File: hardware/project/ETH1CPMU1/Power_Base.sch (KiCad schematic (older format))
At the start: 16 parts, among them Q501 IRFR5410, U501 LM1117IMP-3.3/NOPB, U502 TSR1-2450, U503 MAX5902

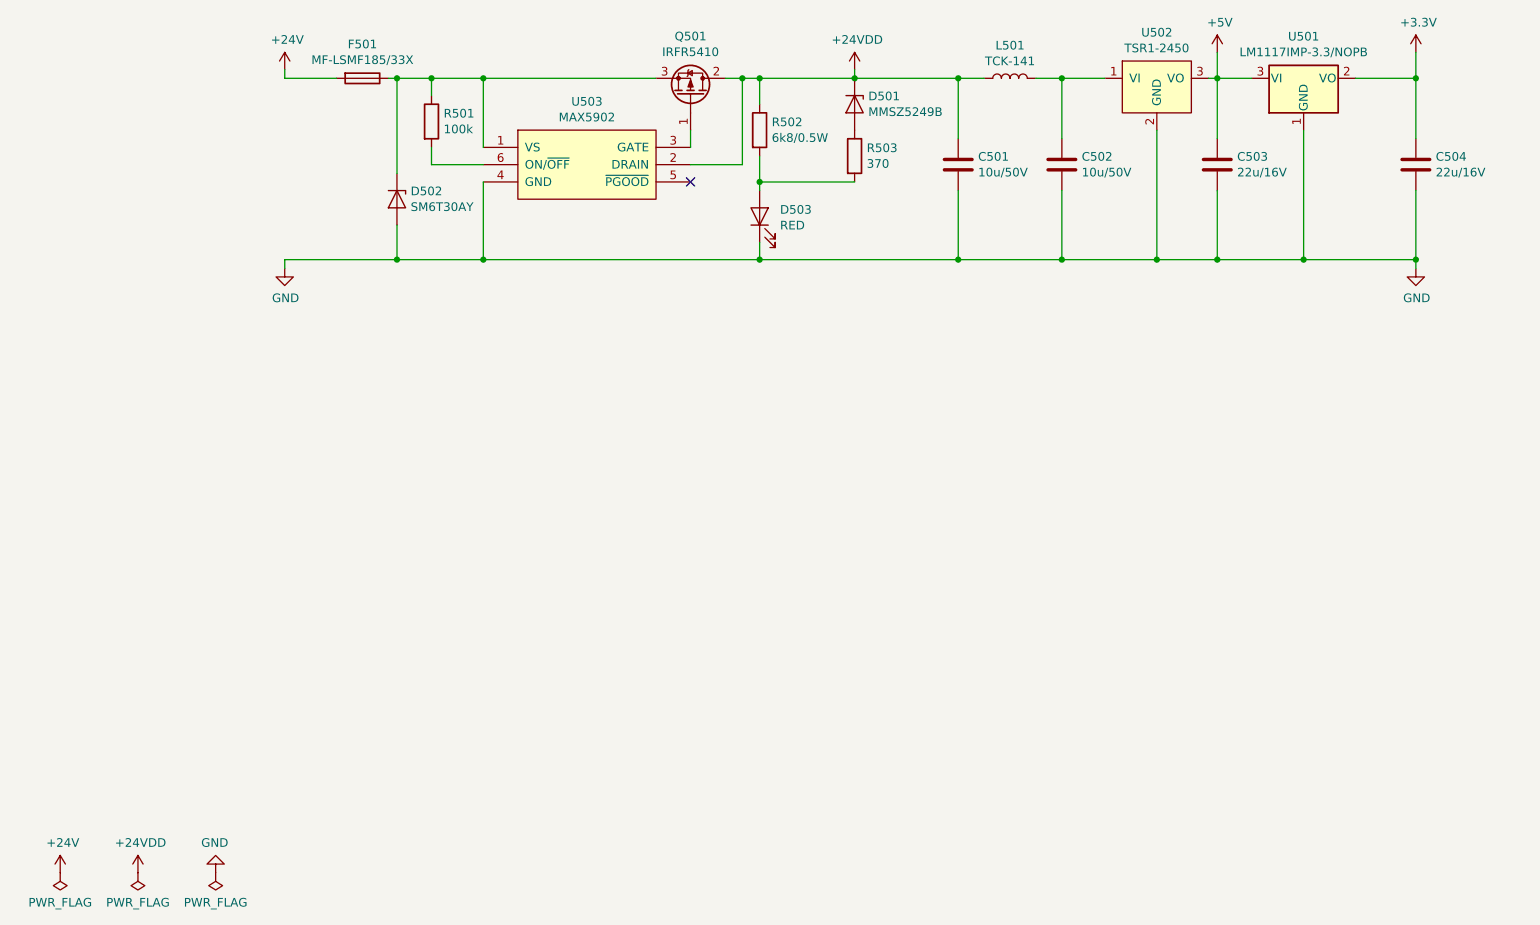
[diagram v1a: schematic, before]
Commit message: Function generator schematic design.
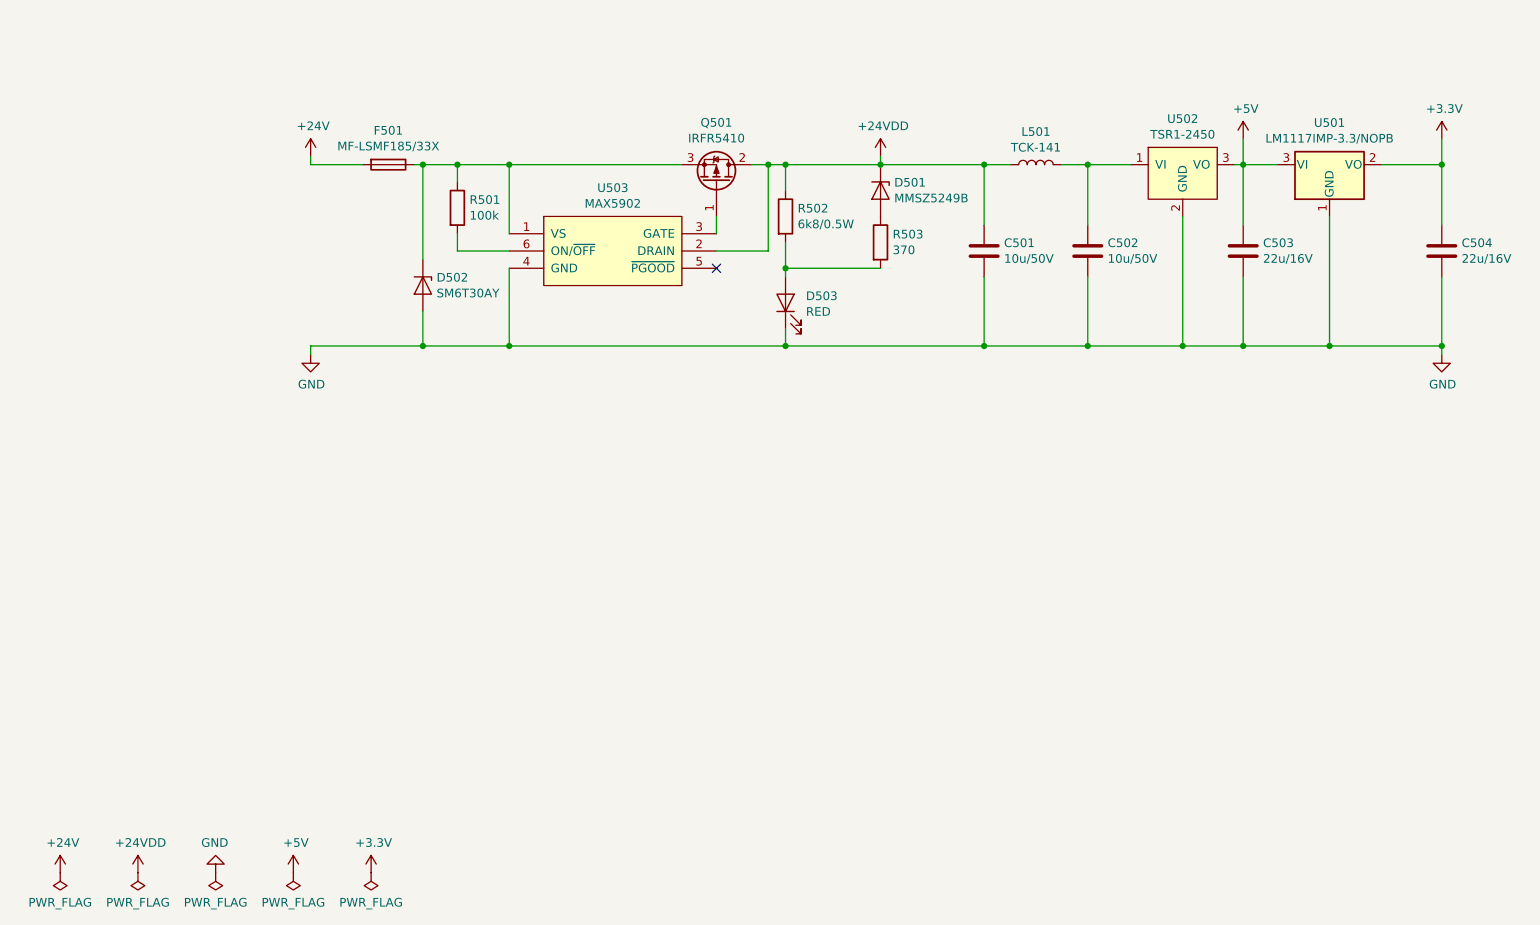
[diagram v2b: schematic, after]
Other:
- moved on the sheet: C501, C502, C503, C504, D501, D502, D503, F501, L501, Q501, R501, R502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

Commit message: Schematic and PCB design.
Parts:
- C501, C502: footprint Capacitor_SMD:C_2220_5650Metric_Pad1.97x5.40mm_HandSolder -> Capacitor_SMD:C_1206_3216Metric_Pad1.42x1.75mm_HandSolder
- C503, C504: value 22u/16V -> 10u/16V; footprint Capacitor_SMD:C_2220_5650Metric_Pad1.97x5.40mm_HandSolder -> Capacitor_SMD:C_1206_3216Metric_Pad1.42x1.75mm_HandSolder
- U502: footprint (none) -> ETH1CPMU1:TSR1

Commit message: Schematic design
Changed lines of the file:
@@
 Wire Wire Line
 	6850 3200 6850 3250
+$Comp
+L power:PWR_FLAG #FLG0502
+U 1 1 5DDE91B3
+P 850 7350
+F 0 "#FLG0502" H 850 7425 50  0001 C CNN
+F 1 "PWR_FLAG" H 850 7523 50  0000 C CNN
+F 2 "" H 850 7350 50  0001 C CNN
+F 3 "~" H 850 7350 50  0001 C CNN
+	1    850  7350
+	-1   0    0    1
+$EndComp
+$Comp
+L power:+24V #PWR0507
+U 1 1 5DDE9577
+P 850 7350
+F 0 "#PWR0507" H 850 7200 50  0001 C CNN
+F 1 "+24V" H 865 7523 50  0000 C CNN
+F 2 "" H 850 7350 50  0001 C CNN
+F 3 "" H 850 7350 50  0001 C CNN
+	1    850  7350
+	1    0    0    -1
+$EndComp
+$Comp
+L power:PWR_FLAG #FLG0503
+U 1 1 5DDF63B9
+P 1300 7350
+F 0 "#FLG0503" H 1300 7425 50  0001 C CNN
+F 1 "PWR_FLAG" H 1300 7523 50  0000 C CNN
+F 2 "" H 1300 7350 50  0001 C CNN
+F 3 "~" H 1300 7350 50  0001 C CNN
+	1    1300 7350
+	-1   0    0    1
+$EndComp
+$Comp
+L power:GND #PWR0508
+U 1 1 5DDF6902
+P 1300 7350
+F 0 "#PWR0508" H 1300 7100 50  0001 C CNN
+F 1 "GND" H 1305 7177 50  0000 C CNN
+F 2 "" H 1300 7350 50  0001 C CNN
+F 3 "" H 1300 7350 50  0001 C CNN
+	1    1300 7350
+	-1   0    0    1
+$EndComp
+$Comp
+L power:PWR_FLAG #FLG0504
+U 1 1 5DDFBB5F
+P 1750 7350
+F 0 "#FLG0504" H 1750 7425 50  0001 C CNN
+F 1 "PWR_FLAG" H 1750 7523 50  0000 C CNN
+F 2 "" H 1750 7350 50  0001 C CNN
+F 3 "~" H 1750 7350 50  0001 C CNN
+	1    1750 7350
+	-1   0    0    1
+$EndComp
+$Comp
+L ETH1CPMU1:+24VDD #PWR0509
+U 1 1 5DDFC0E6
+P 1750 7350
+F 0 "#PWR0509" H 1750 7200 50  0001 C CNN
+F 1 "+24VDD" H 1765 7523 50  0000 C CNN
+F 2 "" H 1750 7350 50  0001 C CNN
+F 3 "" H 1750 7350 50  0001 C CNN
+	1    1750 7350
+	1    0    0    -1
+$EndComp
 $EndSCHEMATC

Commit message: PCB design
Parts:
- renumbered D502 to D501, D503 to D502, D501 to D503, U503 to U501, U501 to U503
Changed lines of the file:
@@
 $Descr A4 11693 8268
 encoding utf-8
-Sheet 5 15
+Sheet 5 16
 Title ""
 Date ""
@@
 	3000 3800 3000 3250
 $Comp
-L Device:D_Zener D502
+L Device:D_Zener D501
 U 1 1 5D70DE79
 P 3000 3950
-F 0 "D502" V 2954 4029 50  0000 L CNN
+F 0 "D501" V 2954 4029 50  0000 L CNN
 F 1 "SM6T30AY" V 3045 4029 50  0000 L CNN
 F 2 "ETH1CPMU1:DO_214AA_REV" H 3000 3950 50  0001 C CNN
@@
 Connection ~ 5100 3850
 $Comp
-L Device:D_Zener D501
+L Device:D_Zener D503
 U 1 1 5D6DFA8C
 P 5650 3400
-F 0 "D501" V 5604 3479 50  0000 L CNN
+F 0 "D503" V 5604 3479 50  0000 L CNN
 F 1 "MMSZ5249B" V 5695 3479 50  0000 L CNN
 F 2 "Diode_SMD:D_SOD-123" H 5650 3400 50  0001 C CNN
@@
 $EndComp
 $Comp
-L Device:LED D503
+L Device:LED D502
 U 1 1 5D6D7414
 P 5100 4050
-F 0 "D503" V 5139 3932 50  0000 R CNN
+F 0 "D502" V 5139 3932 50  0000 R CNN
 F 1 "RED" V 5048 3932 50  0000 R CNN
 F 2 "LED_SMD:LED_0603_1608Metric_Pad1.05x0.95mm_HandSolder" H 5100 4050 50  0001 C CNN
@@
 $EndComp
 $Comp
-L power:+24V #PWR0503
+L power:+24V #PWR0504
 U 1 1 5D7B3705
 P 2350 3200
-F 0 "#PWR0503" H 2350 3050 50  0001 C CNN
+F 0 "#PWR0504" H 2350 3050 50  0001 C CNN
 F 1 "+24V" H 2365 3373 50  0000 C CNN
 F 2 "" H 2350 3200 50  0001 C CNN
@@
 	3000 3250 3200 3250
 $Comp
-L ETH1CPMU1:MAX5902 U503
+L ETH1CPMU1:MAX5902 U501
 U 1 1 5D6EBA14
 P 4100 3750
-F 0 "U503" H 4100 4115 50  0000 C CNN
+F 0 "U501" H 4100 4115 50  0000 C CNN
 F 1 "MAX5902" H 4100 4024 50  0000 C CNN
 F 2 "Package_TO_SOT_SMD:SOT-23-6_Handsoldering" H 4100 3750 60  0001 C CNN
@@
 Connection ~ 5100 4300
 $Comp
-L ETH1CPMU1:+24VDD #PWR0504
+L ETH1CPMU1:+24VDD #PWR0506
 U 1 1 5DA9B429
 P 5650 3200
-F 0 "#PWR0504" H 5650 3050 50  0001 C CNN
+F 0 "#PWR0506" H 5650 3050 50  0001 C CNN
 F 1 "+24VDD" H 5665 3373 50  0000 C CNN
 F 2 "" H 5650 3200 50  0001 C CNN
@@
 	7750 3100 7750 3250
 $Comp
-L power:+5V #PWR0501
+L power:+5V #PWR0507
 U 1 1 5DD09470
 P 7750 3100
-F 0 "#PWR0501" H 7750 2950 50  0001 C CNN
+F 0 "#PWR0507" H 7750 2950 50  0001 C CNN
 F 1 "+5V" H 7765 3273 50  0000 C CNN
 F 2 "" H 7750 3100 50  0001 C CNN
@@
 	8900 3100 8900 3250
 $Comp
-L power:+3.3V #PWR0502
+L power:+3.3V #PWR0508
 U 1 1 5DA96AF7
 P 8900 3100
-F 0 "#PWR0502" H 8900 2950 50  0001 C CNN
+F 0 "#PWR0508" H 8900 2950 50  0001 C CNN
 F 1 "+3.3V" H 8915 3273 50  0000 C CNN
 F 2 "" H 8900 3100 50  0001 C CNN
@@
 $EndComp
 $Comp
-L Regulator_Linear:LM1117-3.3 U501
+L Regulator_Linear:LM1117-3.3 U503
 U 1 1 5DAAA77C
 P 8250 3250
-F 0 "U501" H 8250 3492 50  0000 C CNN
+F 0 "U503" H 8250 3492 50  0000 C CNN
 F 1 "LM1117IMP-3.3/NOPB" H 8250 3401 50  0000 C CNN
 F 2 "Package_TO_SOT_SMD:SOT-223-3_TabPin2" H 8250 3250 50  0001 C CNN
@@
 $EndComp
 $Comp
-L power:GND #PWR0506
+L power:GND #PWR0509
 U 1 1 5DAA429A
 P 8900 4350
-F 0 "#PWR0506" H 8900 4100 50  0001 C CNN
+F 0 "#PWR0509" H 8900 4100 50  0001 C CNN
 F 1 "GND" H 8905 4177 50  0000 C CNN
 F 2 "" H 8900 4350 50  0001 C CNN
@@
 	6850 3250 7100 3250
 $Comp
-L power:PWR_FLAG #FLG0501
+L power:PWR_FLAG #FLG0504
 U 1 1 5E5270F4
 P 6850 3200
-F 0 "#FLG0501" H 6850 3275 50  0001 C CNN
+F 0 "#FLG0504" H 6850 3275 50  0001 C CNN
 F 1 "PWR_FLAG" H 6850 3373 50  0000 C CNN
 F 2 "" H 6850 3200 50  0001 C CNN
@@
 	6850 3200 6850 3250
 $Comp
-L power:PWR_FLAG #FLG0502
+L power:PWR_FLAG #FLG0501
 U 1 1 5DDE91B3
 P 850 7350
-F 0 "#FLG0502" H 850 7425 50  0001 C CNN
+F 0 "#FLG0501" H 850 7425 50  0001 C CNN
 F 1 "PWR_FLAG" H 850 7523 50  0000 C CNN
 F 2 "" H 850 7350 50  0001 C CNN
@@
 $EndComp
 $Comp
-L power:+24V #PWR0507
+L power:+24V #PWR0501
 U 1 1 5DDE9577
 P 850 7350
-F 0 "#PWR0507" H 850 7200 50  0001 C CNN
+F 0 "#PWR0501" H 850 7200 50  0001 C CNN
 F 1 "+24V" H 865 7523 50  0000 C CNN
 F 2 "" H 850 7350 50  0001 C CNN
@@
 $EndComp
 $Comp
-L power:PWR_FLAG #FLG0503
+L power:PWR_FLAG #FLG0502
 U 1 1 5DDF63B9
 P 1300 7350
-F 0 "#FLG0503" H 1300 7425 50  0001 C CNN
+F 0 "#FLG0502" H 1300 7425 50  0001 C CNN
 F 1 "PWR_FLAG" H 1300 7523 50  0000 C CNN
 F 2 "" H 1300 7350 50  0001 C CNN
@@
 $EndComp
 $Comp
-L power:GND #PWR0508
+L power:GND #PWR0502
 U 1 1 5DDF6902
 P 1300 7350
-F 0 "#PWR0508" H 1300 7100 50  0001 C CNN
+F 0 "#PWR0502" H 1300 7100 50  0001 C CNN
 F 1 "GND" H 1305 7177 50  0000 C CNN
 F 2 "" H 1300 7350 50  0001 C CNN
@@
 $EndComp
 $Comp
-L power:PWR_FLAG #FLG0504
+L power:PWR_FLAG #FLG0503
 U 1 1 5DDFBB5F
 P 1750 7350
-F 0 "#FLG0504" H 1750 7425 50  0001 C CNN
+F 0 "#FLG0503" H 1750 7425 50  0001 C CNN
 F 1 "PWR_FLAG" H 1750 7523 50  0000 C CNN
 F 2 "" H 1750 7350 50  0001 C CNN
@@
 $EndComp
 $Comp
-L ETH1CPMU1:+24VDD #PWR0509
+L ETH1CPMU1:+24VDD #PWR0503
 U 1 1 5DDFC0E6
 P 1750 7350
-F 0 "#PWR0509" H 1750 7200 50  0001 C CNN
+F 0 "#PWR0503" H 1750 7200 50  0001 C CNN
 F 1 "+24VDD" H 1765 7523 50  0000 C CNN
 F 2 "" H 1750 7350 50  0001 C CNN
